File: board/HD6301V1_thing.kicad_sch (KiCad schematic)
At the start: 28 parts, among them J1 USB_B_Micro, SW1 Reset, U1 74HC00, U2 APX811-46, U3 FT231XS, U4 HD6301V1, U5 CD4053B, U6 74HCT573, U7 AS7C256B, U8 28C256, X1 CXO_DIP14

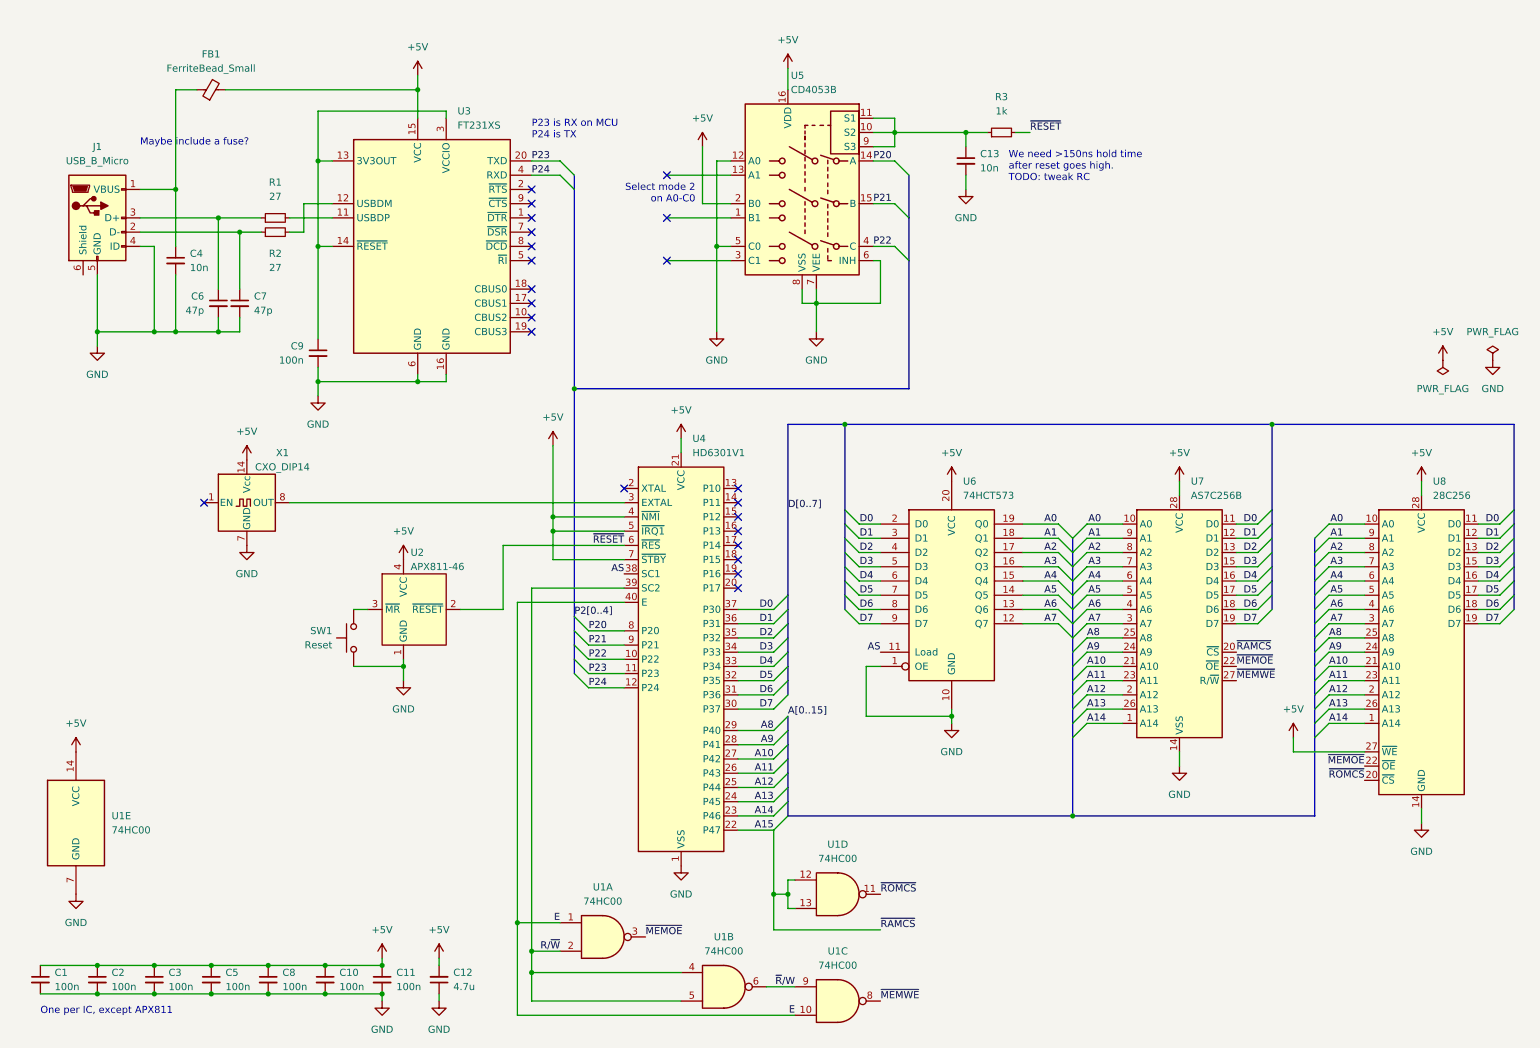
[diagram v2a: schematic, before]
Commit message: Mostly finished schematic and fully routed board - a few TODOs remaining
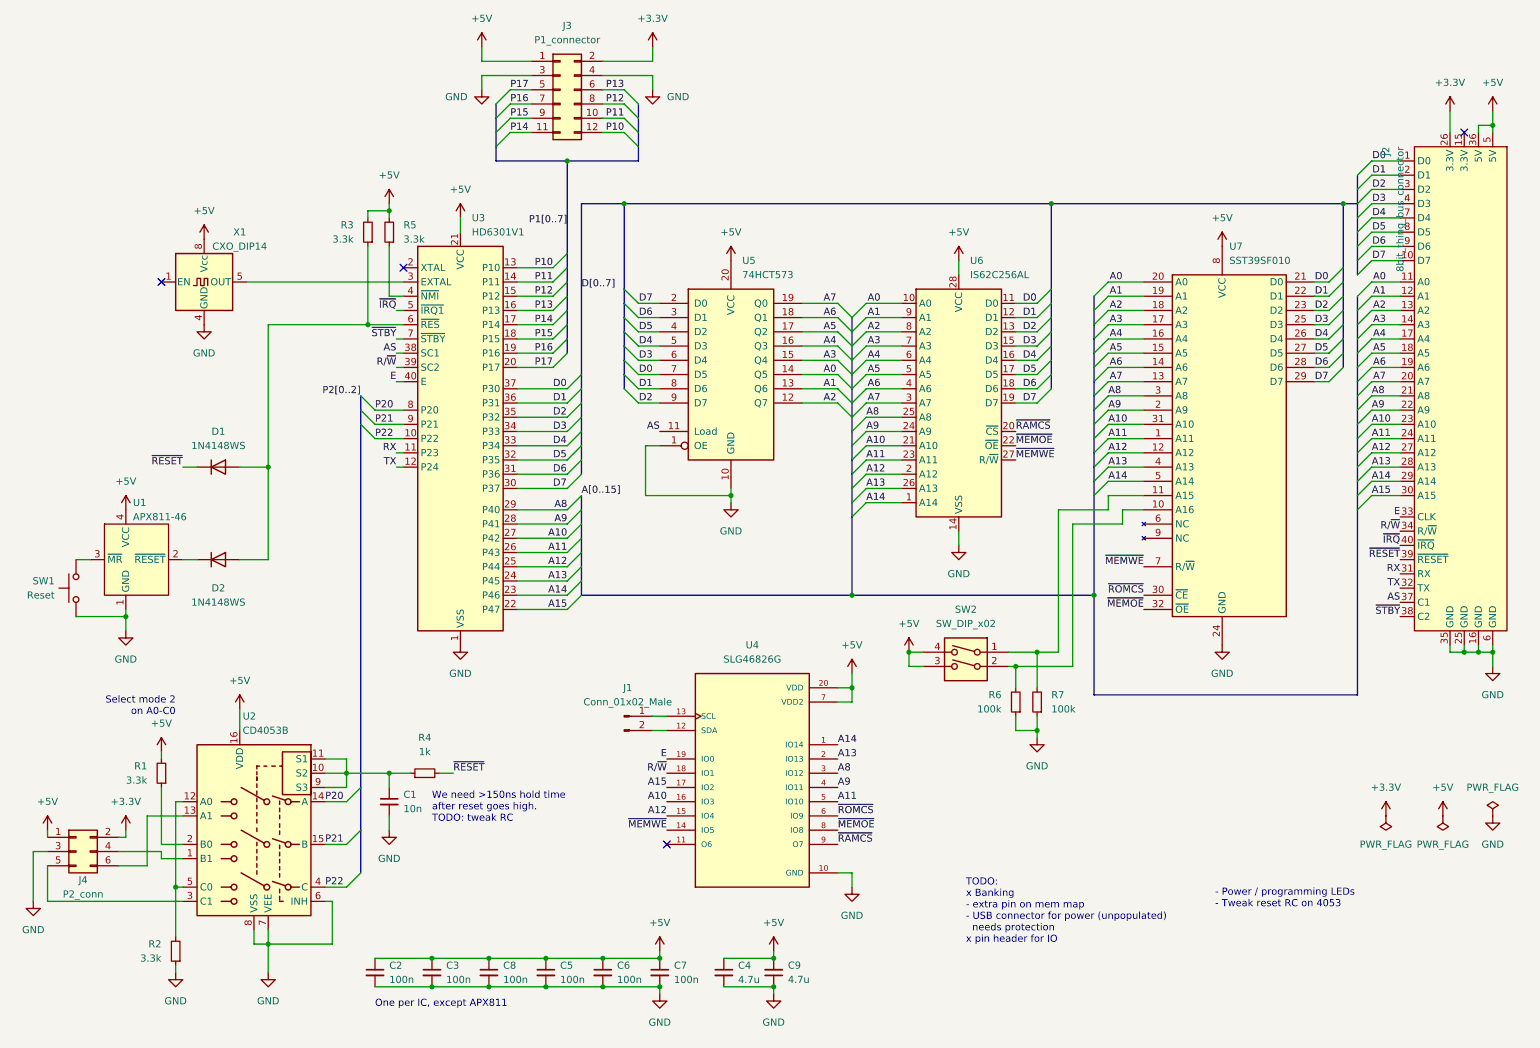
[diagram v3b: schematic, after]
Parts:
- removed C4: 10n, symbol Device:C_Small
- removed C6, C7: 47p, symbol Device:C_Small
- removed C9: 100n, symbol Device:C_Small
- removed FB1: FerriteBead_Small, symbol Device:FerriteBead_Small
- removed J1: USB_B_Micro, symbol Connector:USB_B_Micro
- removed U1: 74HC00, symbol 74xx:74HC00
- removed U3: FT231XS, Package_SO:SSOP-20_3.9x8.7mm_P0.635mm, symbol Interface_USB:FT231XS
- removed U8: 28C256, symbol Memory_EEPROM:28C256
- added D1, D2: 1N4148WS, Diode_SMD:D_SOD-323, symbol Diode:1N4148WS
- added J1: Conn_01x02_Male, Connector_PinHeader_2.54mm:PinHeader_1x02_P2.54mm_Vertical, symbol Connector:Conn_01x02_Male
- added J2: 8bit_thing_bus_connector, Connector_IDC:IDC-Header_2x20_P2.54mm_Horizontal, symbol own_symbols:8bit_thing_bus_connector
- added J3: P1_connector, Connector_PinHeader_2.54mm:PinHeader_2x06_P2.54mm_Horizontal, symbol Connector_Generic:Conn_02x06_Odd_Even
- added J4: P2_conn, Connector_PinHeader_2.54mm:PinHeader_2x03_P2.54mm_Horizontal, symbol Connector_Generic:Conn_02x03_Odd_Even
- added R3, R5: 3.3k, Resistor_SMD:R_0805_2012Metric_Pad1.20x1.40mm_HandSolder, symbol Device:R_Small
- added R6, R7: 100k, Resistor_SMD:R_0805_2012Metric_Pad1.20x1.40mm_HandSolder, symbol Device:R_Small
- added SW2: SW_DIP_x02, imported_footprints:SW_DS04-254-1L-02BK, symbol Switch:SW_DIP_x02
- added U4: SLG46826G, Package_SO:TSSOP-20_4.4x6.5mm_P0.65mm, symbol imported_symbols:SLG46826G
- added U7: SST39SF010, Package_SO:TSOP-I-32_12.4x8mm_P0.5mm, symbol own_symbols:SST39SF010A-TSOP-PINOUT
- C1: renamed from C13; footprint (none) -> Capacitor_SMD:C_0805_2012Metric_Pad1.18x1.45mm_HandSolder
- C2: renamed from C1; footprint (none) -> Capacitor_SMD:C_0805_2012Metric_Pad1.18x1.45mm_HandSolder
- C3: renamed from C2; footprint (none) -> Capacitor_SMD:C_0805_2012Metric_Pad1.18x1.45mm_HandSolder
- C4: renamed from C11; value 100n -> 4.7u; footprint (none) -> Capacitor_SMD:C_0805_2012Metric_Pad1.18x1.45mm_HandSolder
- C5: footprint (none) -> Capacitor_SMD:C_0805_2012Metric_Pad1.18x1.45mm_HandSolder
- C6: renamed from C8; footprint (none) -> Capacitor_SMD:C_0805_2012Metric_Pad1.18x1.45mm_HandSolder
- C7: renamed from C10; footprint (none) -> Capacitor_SMD:C_0805_2012Metric_Pad1.18x1.45mm_HandSolder
- C8: renamed from C3; footprint (none) -> Capacitor_SMD:C_0805_2012Metric_Pad1.18x1.45mm_HandSolder
- C9: renamed from C12; footprint (none) -> Capacitor_SMD:C_0805_2012Metric_Pad1.18x1.45mm_HandSolder
- R1, R2: value 27 -> 3.3k; footprint (none) -> Resistor_SMD:R_0805_2012Metric_Pad1.20x1.40mm_HandSolder
- R4: renamed from R3; footprint (none) -> Resistor_SMD:R_0805_2012Metric_Pad1.20x1.40mm_HandSolder
- SW1: footprint (none) -> Button_Switch_SMD:SW_SPST_TL3305A
- U2: renamed from U5; footprint (none) -> Package_SO:SOIC-16_3.9x9.9mm_P1.27mm
- U5: renamed from U6; footprint (none) -> Package_SO:SOIC-20W_7.5x12.8mm_P1.27mm
- U6: renamed from U7; value AS7C256B -> IS62C256AL; footprint Package_DIP:DIP-28_W15.24mm -> imported_footprints:SOIC127P1210X305-28N
- X1: footprint Oscillator:Oscillator_DIP-14 -> Oscillator:Oscillator_DIP-8; symbol Oscillator:CXO_DIP14 -> Oscillator:CXO_DIP8
- renumbered U2 to U1, U4 to U3
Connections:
- net +5V: now also R1.2, X1.8 (Vcc), J2.36 (5V), J2.5 (5V), J3.1 (Pin_1), J4.1 (Pin_1), R3.2, R5.2, SW2.3, SW2.4, U4.20 (VDD), U4.7 (VDD2), U7.8 (VCC); no longer U2.2 (B0), U3.4 (~{NMI}), U3.5 (~{IRQ1}), U3.7 (~{STBY}), X1.14 (Vcc)
- net A0: now also U5.14 (Q5), J2.11 (A0), U7.20 (A0); no longer U5.19 (Q0)
- net A1: now also U5.13 (Q6), J2.12 (A1), U7.19 (A1); no longer U5.18 (Q1)
- net A10: now also J2.23 (A10), U4.16 (IO3), U7.31 (A10)
- net A11: now also J2.24 (A11), U4.5 (IO10), U7.1 (A11)
- net A12: now also J2.27 (A12), U4.15 (IO4), U7.12 (A12)
- net A13: now also J2.28 (A13), U4.2 (IO13), U7.4 (A13)
- net A14: now also J2.29 (A14), U4.1 (IO14), U7.5 (A14)
- net A15: now also J2.30 (A15), U4.17 (IO2); no longer U6.20 (~{CS})
- net A2: now also U5.12 (Q7), J2.13 (A2), U7.18 (A2); no longer U5.17 (Q2)
- net A3: now also U5.15 (Q4), J2.14 (A3), U7.17 (A3); no longer U5.16 (Q3)
- net A4: now also U5.16 (Q3), J2.17 (A4), U7.16 (A4); no longer U5.15 (Q4)
- net A5: now also U5.17 (Q2), J2.18 (A5), U7.15 (A5); no longer U5.14 (Q5)
- net A6: now also U5.18 (Q1), J2.19 (A6), U7.14 (A6); no longer U5.13 (Q6)
- net A7: now also U5.19 (Q0), J2.20 (A7), U7.13 (A7); no longer U5.12 (Q7)
- net A8: now also J2.21 (A8), U4.3 (IO12), U7.3 (A8)
- net A9: now also J2.22 (A9), U4.4 (IO11), U7.2 (A9)
- net AS: now also J2.37 (C1)
- net D0: now also U5.7 (D5), J2.1 (D0), U7.21 (D0); no longer U5.2 (D0)
- net D1: now also U5.8 (D6), J2.2 (D1), U7.22 (D1); no longer U5.3 (D1)
- net D2: now also U5.9 (D7), J2.3 (D2), U7.23 (D2); no longer U5.4 (D2)
- net D3: now also U5.6 (D4), J2.4 (D3), U7.25 (D3); no longer U5.5 (D3)
- net D4: now also U5.5 (D3), J2.7 (D4), U7.26 (D4); no longer U5.6 (D4)
- net D5: now also U5.4 (D2), J2.8 (D5), U7.27 (D5); no longer U5.7 (D5)
- net D6: now also U5.3 (D1), J2.9 (D6), U7.28 (D6); no longer U5.8 (D6)
- net D7: now also U5.2 (D0), J2.10 (D7), U7.29 (D7); no longer U5.9 (D7)
- net E: now also J2.33 (CLK), U4.19 (IO0)
- net GND: now also R2.1, X1.4 (GND), J2.16 (GND), J2.25 (GND), J2.35 (GND), J2.6 (GND), J3.3 (Pin_3), J3.4 (Pin_4), J4.3 (Pin_3), R6.1, R7.1, U4.10 (GND), U7.24 (GND); no longer U2.12 (A0), U2.5 (C0), X1.7 (GND)
- net R/~{W}: now also J2.34 (R/~{W}), U4.18 (IO1)
- net ~{MEMOE}: now also U4.8 (IO8), U7.32 (~{OE})
- net ~{MEMWE}: now also U4.14 (IO5), U7.7 (R/~{W})
- net ~{RESET}: now also D1.1 (K), J2.39 (~{RESET}); no longer U1.2 (~{RESET}), U3.6 (~{RES})
- net ~{ROMCS}: now also U4.6 (IO9), U7.30 (~{CE})
- net at U3.3 (EXTAL): now also X1.5 (OUT); no longer X1.8 (OUT)
- net at R2.2: now also U2.12 (A0), U2.5 (C0)
- net at U2.1 (B1): now also J4.4 (Pin_4)
- net at U2.13 (A1): now also J4.6 (Pin_6)
- net at U2.3 (C1): now also J4.5 (Pin_5)
- net at R1.1: now also U2.2 (B0)
- net P10: now reaches U3.13 (P10)
- net P10: now also J3.12 (Pin_12)
- net P11: now reaches U3.14 (P11)
- net P11: now also J3.10 (Pin_10)
- net P12: now reaches U3.15 (P12)
- net P12: now also J3.8 (Pin_8)
- net P13: now reaches U3.16 (P13)
- net P13: now also J3.6 (Pin_6)
- net P14: now reaches U3.17 (P14)
- net P14: now also J3.11 (Pin_11)
- net P15: now reaches U3.18 (P15)
- net P15: now also J3.9 (Pin_9)
- net P16: now reaches U3.19 (P16)
- net P16: now also J3.7 (Pin_7)
- net P17: now reaches U3.20 (P17)
- net P17: now also J3.5 (Pin_5)
- net P23 renamed RX
- net RX: now also J2.31 (RX)
- net P24 renamed TX
- net TX: now also J2.32 (TX)
- new net: D2.1 (K), U1.2 (~{RESET})
- new net: D1.2 (A), D2.2 (A), R3.1, U3.6 (~{RES})
- new net: R6.2, SW2.2, U7.10 (A16)
- new net: J1.1 (Pin_1), U4.13 (SCL)
- new net: J1.2 (Pin_2), U4.12 (SDA)
- new net: R7.2, SW2.1, U7.11 (A15)
- new net: R5.1, U3.4 (~{NMI})
- new net +3.3V: J2.26 (3.3V), J3.2 (Pin_2), J4.2 (Pin_2)
- new net ~{IRQ}: J2.40 (~{IRQ}), U3.5 (~{IRQ1})
- new net ~{RAMCS}: U4.9 (O7), U6.20 (~{CS})
- new net ~{STBY}: J2.38 (C2), U3.7 (~{STBY})
- no-connect marks 23 -> 4
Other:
- note added: "- Power / programming LEDs - Tweak reset RC on 4053"
- note added: "TODO: x Banking - extra pin on mem map - USB connector for power (unpopulated) needs protection x pin header for IO"
- note removed: "Maybe include a fuse?"
- note removed: "P23 is RX on MCU P24 is TX"
- moved on the sheet: C1, C2, C3, C4, C5, C6, C7, C8, C9, R4, SW1, U1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

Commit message: Add a TODO for i2c pullups in board schematic
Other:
- note added: "- Power / programming LEDs - Tweak reset RC on 4053 - i2c pullups on greenpak"
- note removed: "- Power / programming LEDs - Tweak reset RC on 4053"
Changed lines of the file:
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@@
     (effects (font (size 1.27 1.27)) (justify right bottom))
   )
-  (text "- Power / programming LEDs\n- Tweak reset RC on 4053"
+  (text "- Power / programming LEDs\n- Tweak reset RC on 4053\n- i2c pullups on greenpak"
     (at 226.06 173.99 0)
     (effects (font (size 1.27 1.27)) (justify left bottom))
